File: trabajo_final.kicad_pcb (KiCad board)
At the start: 2 copper layers, 85.7 x 137.2 mm, 40 parts, among them J1 TB_1X2, P2 CONN_02X01, Q1 2N7002, Q2 2N7002, Q3 2N7002, Q4 2N7002, U1 24LC64, U2 LM2596, U3 NCP1117ST33T3G, U4 Buzzer

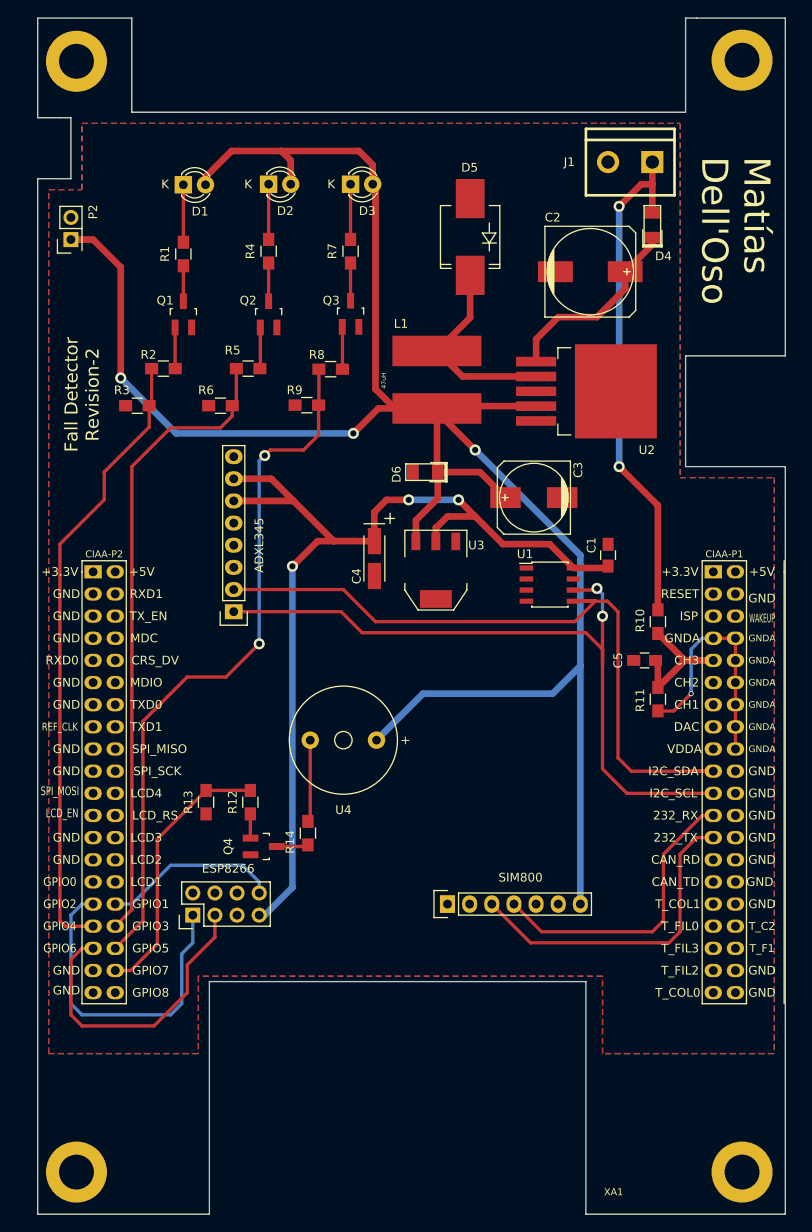
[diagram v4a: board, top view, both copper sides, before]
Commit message: Realizando las correcciones correspondientes a la Revision 1
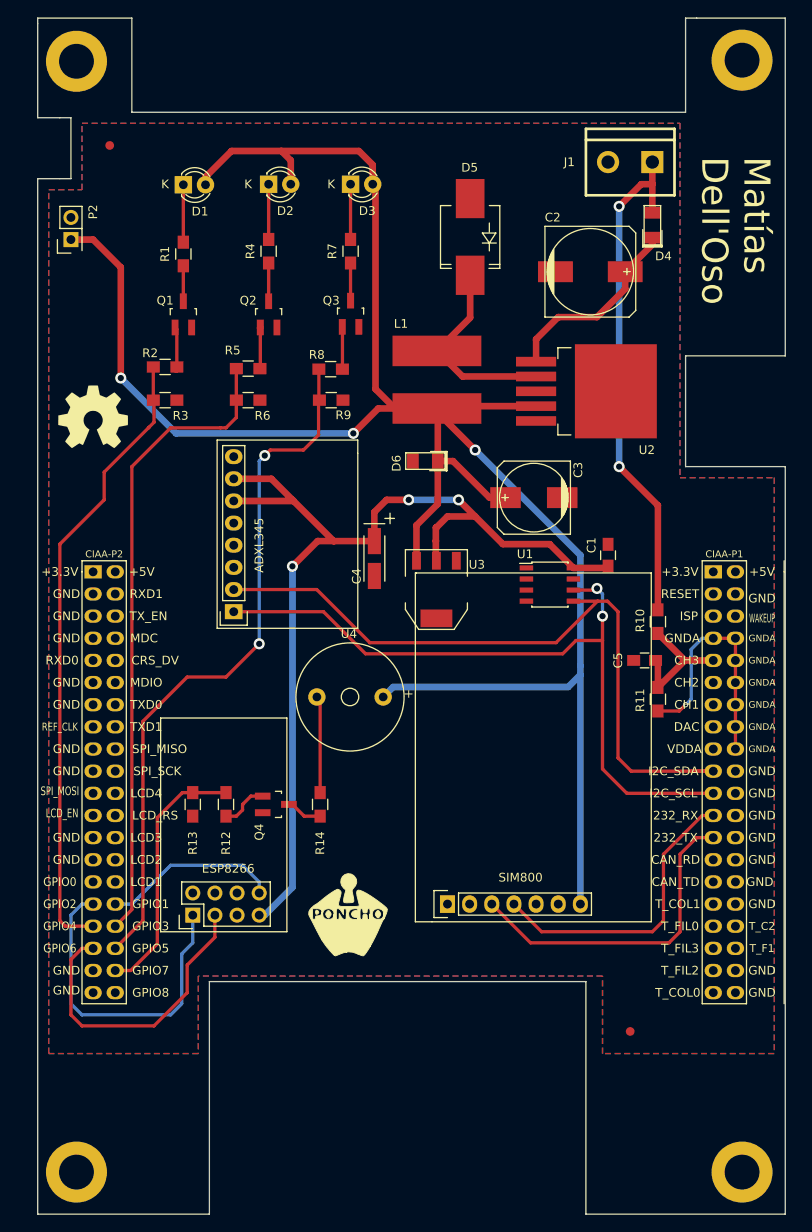
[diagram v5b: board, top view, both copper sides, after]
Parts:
- added F1: FIDUCIAL, footprints:Fiducial_1mm, F.Cu at (81.9, 40.0)
- added F2: FIDUCIAL, footprints:Fiducial_1mm, F.Cu at (141.6, 141.6)
- added G***: LOGO, footprints:Logo_Poncho, F.Cu at (109.2, 128.3)
- added G101: Logo_OSHWA, footprints:Logo_OSHWA, F.Cu at (80.0, 71.1)
- ADXL345: footprint Pin_Headers:Pin_Header_Straight_1x08 -> footprints:adxl345
- ESP8266: footprint Pin_Headers:Pin_Header_Straight_2x04 -> footprints:esp8266
- SIM800: footprint Pin_Headers:Pin_Header_Straight_1x07 -> footprints:sim800l
- moved Q4 5.02 mm to (101.0, 115.6)
- moved U4 5.01 mm to (109.5, 103.3)
- moved R14 3.59 mm to (106.0, 115.6)
- moved R6 3.24 mm to (97.8, 69.2), turned to 180 degrees
- moved R3 3.24 mm to (88.3, 69.2), turned to 180 degrees
- moved R9 2.85 mm to (107.3, 69.2), turned to 180 degrees
- moved R12 2.81 mm to (95.2, 115.6)
- moved U3 2.22 mm to (119.4, 90.9)
- moved R13 1.55 mm to (91.4, 115.6)
- moved D6 1.27 mm to (118.1, 76.2)
- moved R2 0.27 mm to (88.3, 65.4)
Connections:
- net /Circuito Principal/3,3VReg renamed VDD
- net /Circuito Principal/5VReg renamed VCC
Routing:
- net Net-(Q4-Pad1): track 2.79 -> 5.54 mm
- net VDD: track 114.7 -> 117.0 mm
- net Net-(R14-Pad1): track 9.43 -> 11.1 mm
- net /Circuito Principal/GPIO7: track 31.1 -> 29.6 mm
- net /Circuito Principal/SCL: track 83.8 -> 82.9 mm
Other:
- board text removed: "Fall Detector Revision-2"

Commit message: Revisión 1.0 terminada
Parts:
- C1, C5: footprint Capacitors_SMD:C_0805_HandSoldering -> footprints:C_0805_HandSoldering
- C2: footprint mod:c2 -> footprints:c2
- C3: footprint mod:c3 -> footprints:c3
- C4: footprint Capacitors_Tantalum_SMD:TantalC_SizeA_EIA-3216_HandSoldering -> footprints:TantalC_SizeA_EIA-3216_HandSoldering
- D1, D2, D3: footprint LEDs:LED-3MM -> footprints:LED-3MM
- D4, D6: footprint mod:SOD123F -> footprints:SOD123F
- D5: footprint mod:SMC_Handsoldering -> footprints:SMC_Handsoldering
- J1: footprint mod:bornier2 -> footprints:bornier2
- L1: footprint mod:SRN1060 -> footprints:SRN1060
- P2: footprint Pin_Headers:Pin_Header_Straight_2x01 -> footprints:Pin_Header_Straight_2x01
- Q1, Q2, Q3, Q4: footprint TO_SOT_Packages_SMD:SOT-23_Handsoldering -> footprints:SOT-23_Handsoldering
- R1, R10, R11, R12, R13, R14, R2, R3, R4, R5, R6, R7, R8, R9: footprint Resistors_SMD:R_0805_HandSoldering -> footprints:R_0805_HandSoldering
- U1: footprint Housings_SOIC:SOIC-8_3.9x4.9mm_Pitch1.27mm -> footprints:SOIC-8_3.9x4.9mm_Pitch1.27mm
- U2: footprint TO_SOT_Packages_SMD:TO-263-5Lead -> footprints:TO-263-5Lead
- U3: footprint TO_SOT_Packages_SMD:SOT-223 -> footprints:SOT-223
- XA1: footprint mod:Conn_Poncho_Completo -> footprints:Conn_Poncho_Completo
- moved F1 3.17 mm to (85.1, 40.0)
- moved G101 2.54 mm to (80.0, 73.7)
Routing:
- net /Circuito Principal/SDA: track 82.7 -> 79.2 mm
- net /Circuito Principal/GPIO5: track 81.0 -> 79.3 mm
- net VDD: track 117.0 -> 117.6 mm, vias 3 -> 6
- net /Circuito Principal/SCL: track 82.9 -> 82.4 mm
- net VCC: track 246.7 -> 246.4 mm, vias 3 -> 4
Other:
- outline, holes or cut-outs redrawn
- board text added: "Material: FR4-Standard Tg 140C"
- board text added: "Máscara antisoldante: arriba y abajo"
- board text added: "Número de capas: 2"
- board text added: "Serigrafía: arriba"
- board text added: "Terminación: HASL"

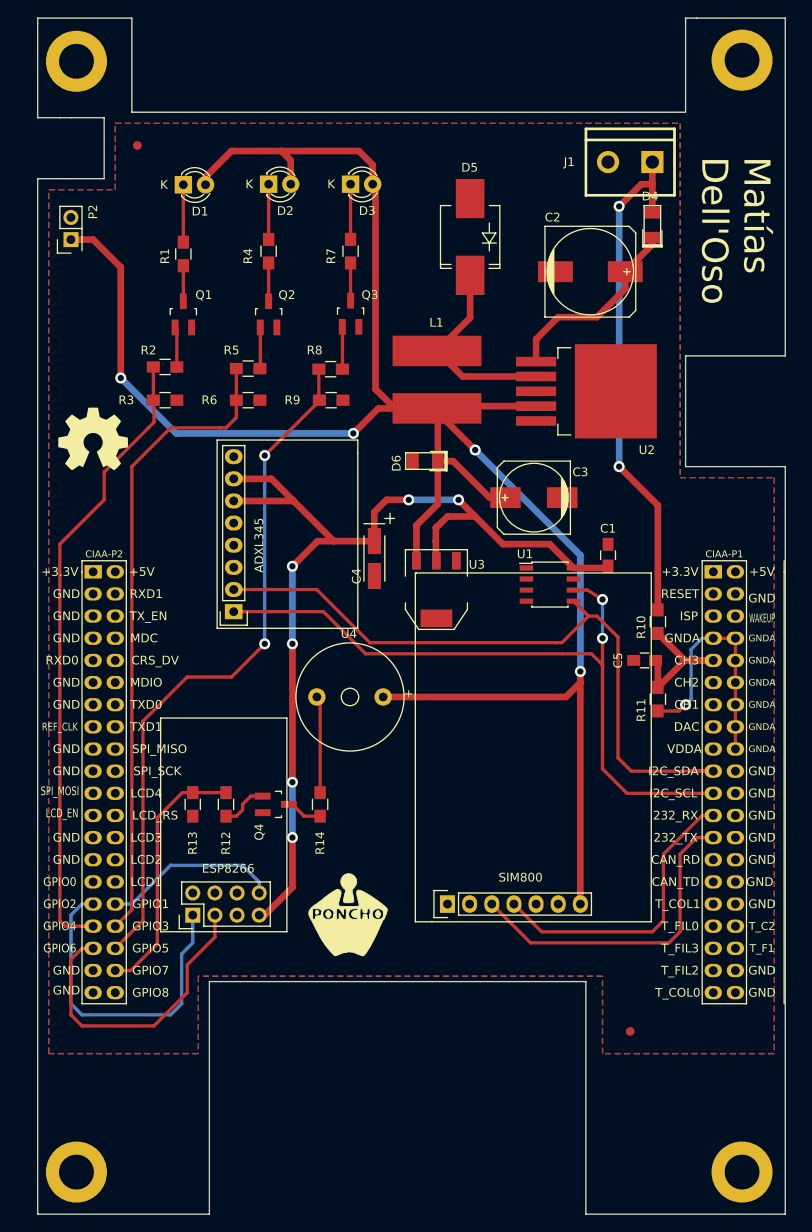
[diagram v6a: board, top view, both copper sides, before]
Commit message: correcciones menores sobre el PCB
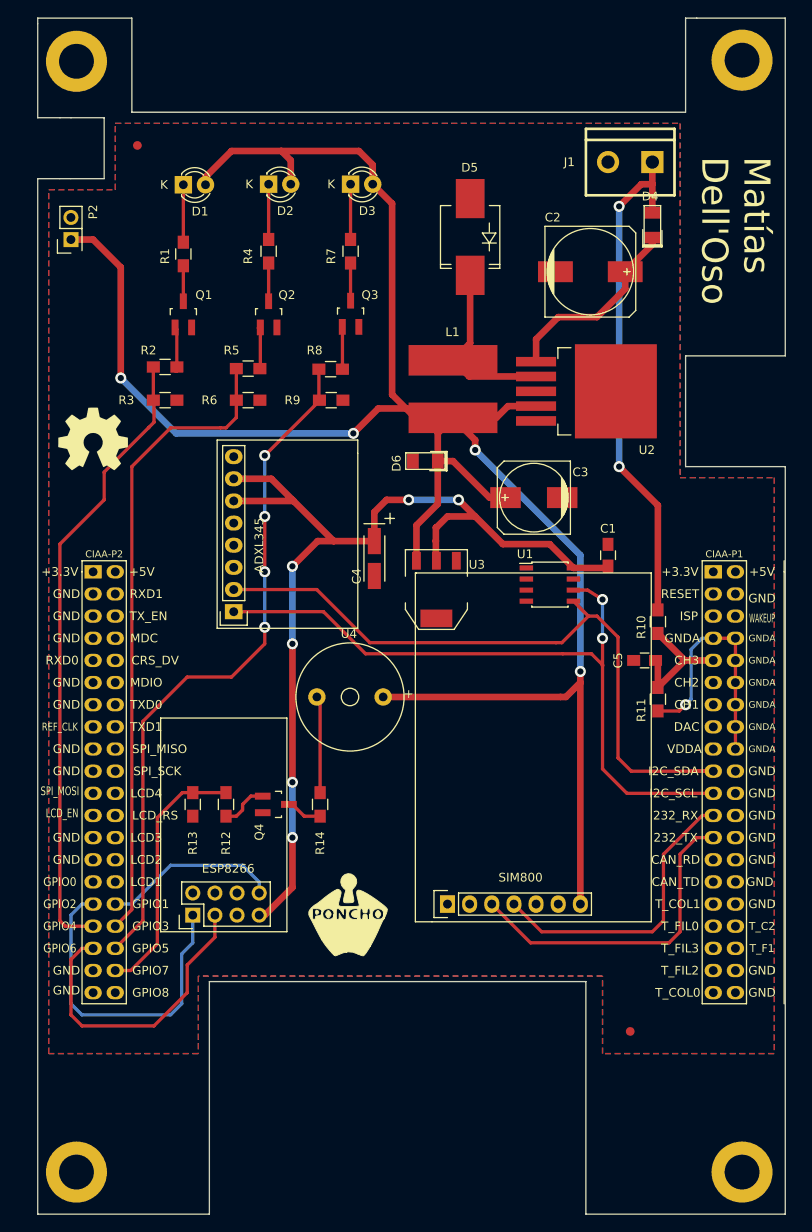
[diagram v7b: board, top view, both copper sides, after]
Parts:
- moved L1 2.13 mm to (121.3, 67.9)
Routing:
- net Net-(D5-Pad2): track 22.8 -> 20.9 mm
- net VCC: track 246.4 -> 247.0 mm
- net /Circuito Principal/GPIO5: vias 2 -> 4
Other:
- board text added: "FALL DETECTOR"
- board text removed: "FALLING DETECTOR"
